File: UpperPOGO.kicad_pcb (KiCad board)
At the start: 2 copper layers, 128 x 58.5 mm, 29 parts, among them J1 Conn_01x01_MountingPin, J10 Conn_01x01_MountingPin, J11 Conn_01x01_MountingPin, J12 Conn_01x01_MountingPin, J13 Conn_01x01_MountingPin, J14 Conn_01x01_MountingPin, J15 Conn_01x01_MountingPin, J16 Conn_01x01_MountingPin, J17 Conn_01x01_MountingPin, J18 Conn_01x01_MountingPin, J19 Conn_01x01_MountingPin, J2 Conn_01x01_MountingPin, J20 Conn_01x01_MountingPin, J21 Conn_01x01_MountingPin, J22 Conn_01x01_MountingPin, J23 Conn_01x01_MountingPin, J24 Conn_01x01_MountingPin, J25 Conn_01x24_Pin, J3 Conn_01x01_MountingPin, J4 Conn_01x01_MountingPin, J5 Conn_01x01_MountingPin, J6 Conn_01x01_MountingPin, J7 Conn_01x01_MountingPin, J8 Conn_01x01_MountingPin, J9 Conn_01x01_MountingPin

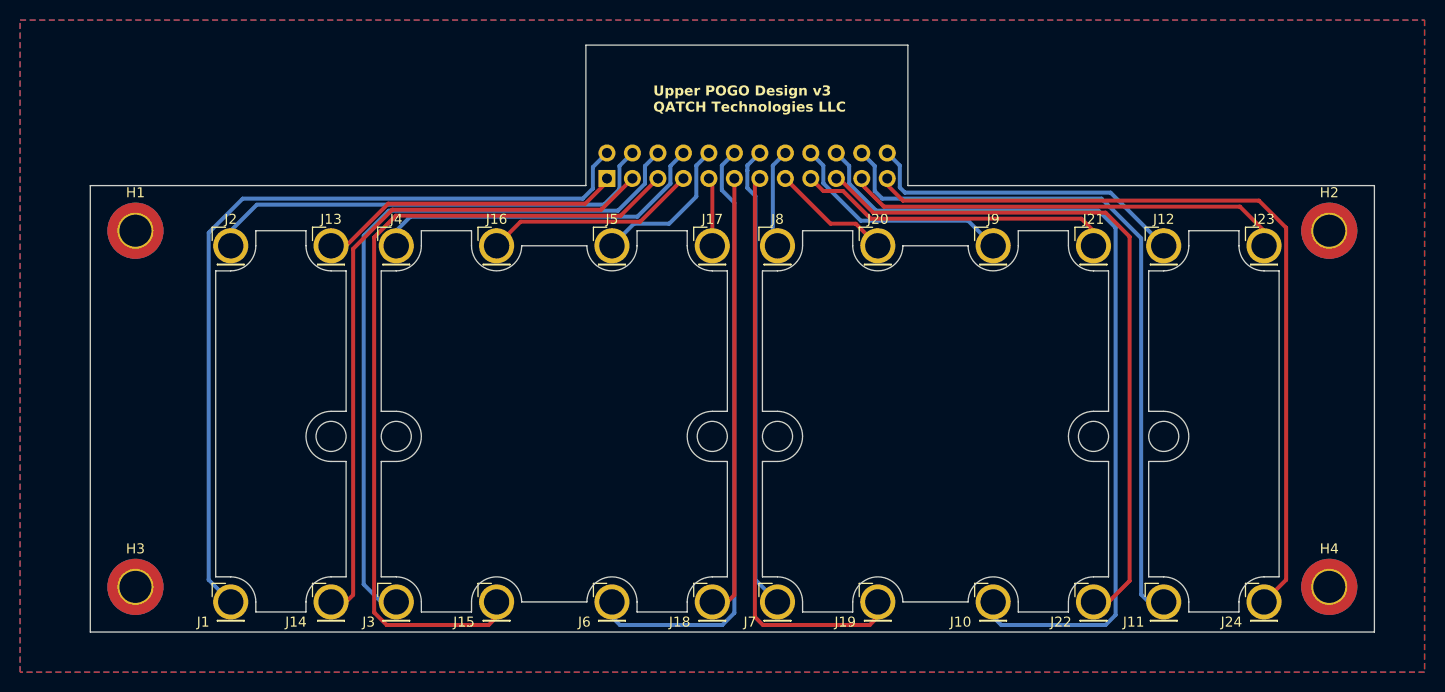
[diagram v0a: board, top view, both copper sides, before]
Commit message: Change footprint on J25 to vertical orientation header Resize PCB to remove unneeded area of horizontal silkscreening for J25 Update fabrication outputs and image renderings
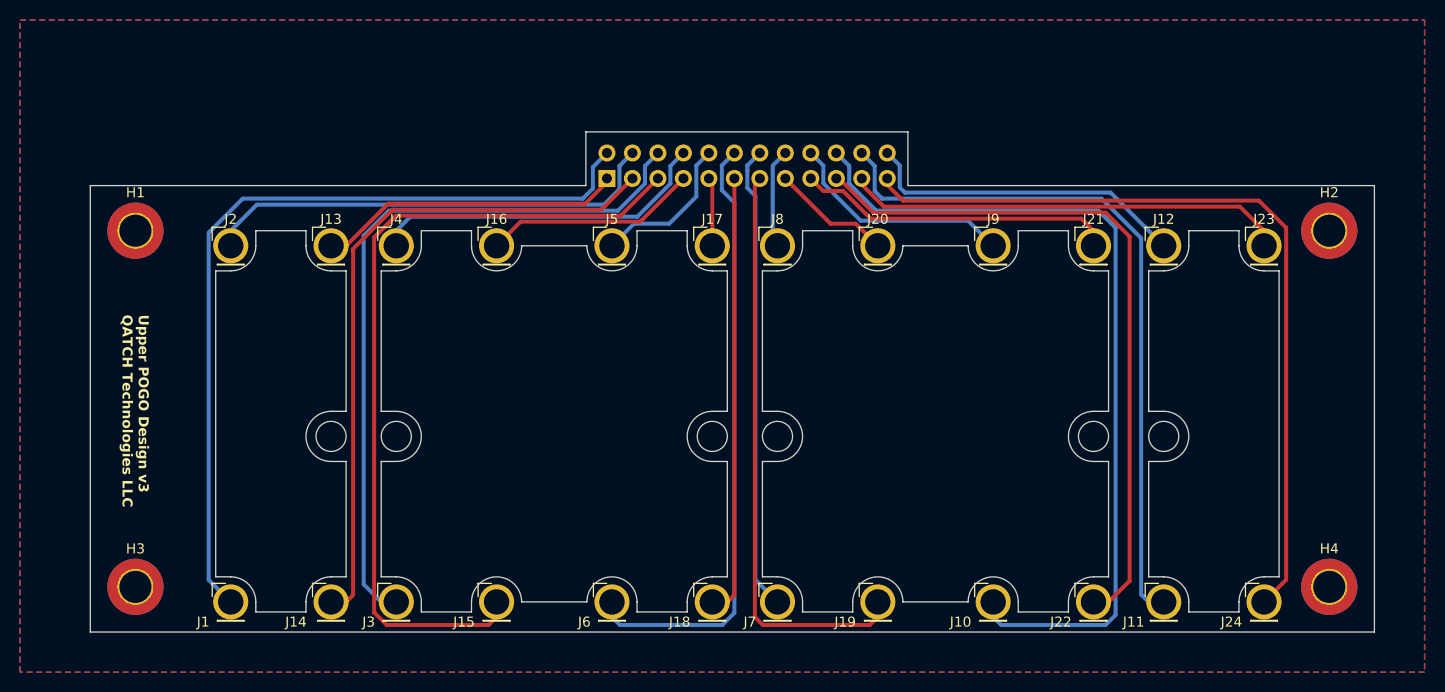
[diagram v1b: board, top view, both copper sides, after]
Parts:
- J25: footprint Connector_PinSocket_2.54mm:PinSocket_2x12_P2.54mm_Horizontal -> Connector_PinSocket_2.54mm:PinSocket_2x12_P2.54mm_Vertical
- moved J25 19.2 mm to (133.5, 60.8), turned to -90 degrees
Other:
- board size 128 x 58.5 mm -> 128 x 49.9 mm

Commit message: UpperPOGO v4 (2024-06-21) Resize J vias for proper fit inner diameter: 2.49mm outer diameter: 3.25mm
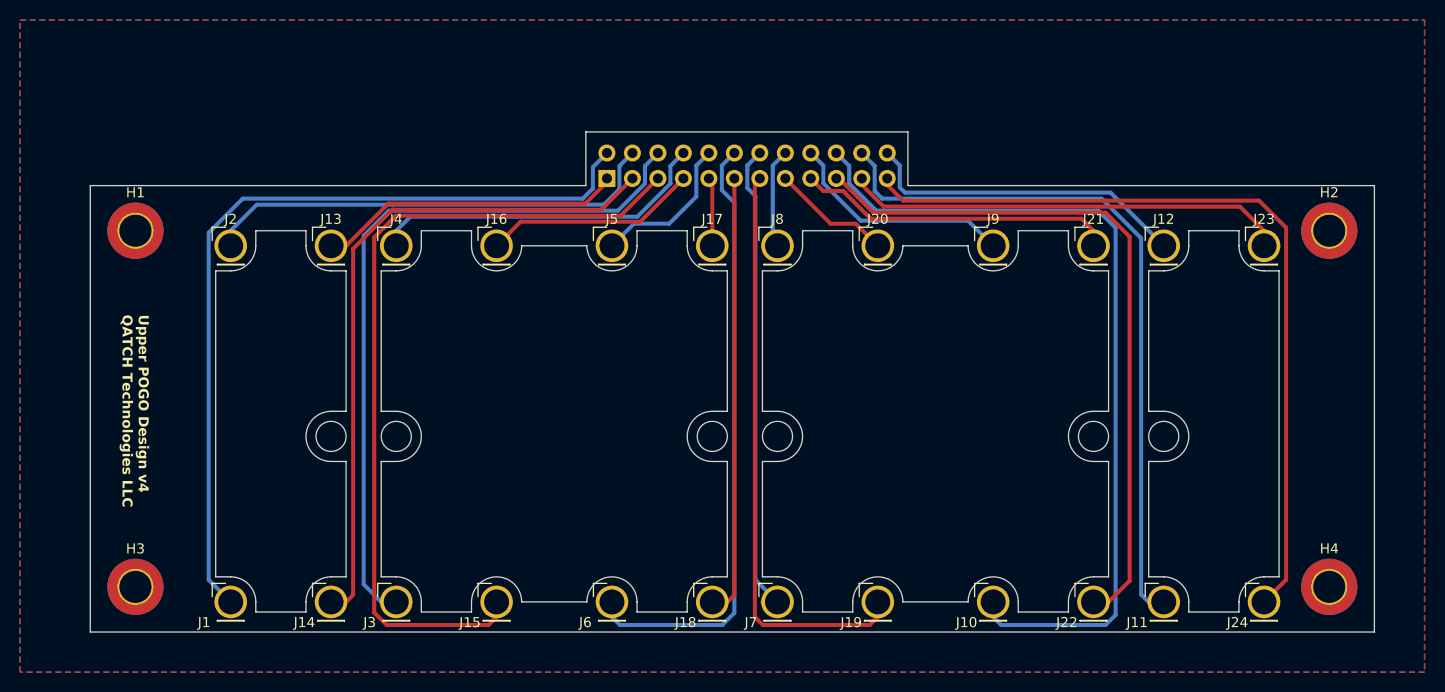
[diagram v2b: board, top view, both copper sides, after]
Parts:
- J1, J10, J11, J12, J13, J14, J15, J16, J17, J18, J19, J2, J20, J21, J22, J23, J24, J3, J4, J5, J6, J7, J8, J9: footprint Connector_PinHeader_2.54mm:PinHeader_1x01_D2.54mm_Vertical -> Connector_PinHeader_2.54mm:PinHeader_1x01_D2.54mm_Vertical_PogoPin
- J25: value Conn_01x24_Pin -> Conn_02x12_Pin
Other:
- board text added: "Upper POGO Design v4 QATCH Technologies LLC"
- board text removed: "Upper POGO Design v3 QATCH Technologies LLC"

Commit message: UpperPOGO v5 1mm trace spacing 1mm POGO clearance
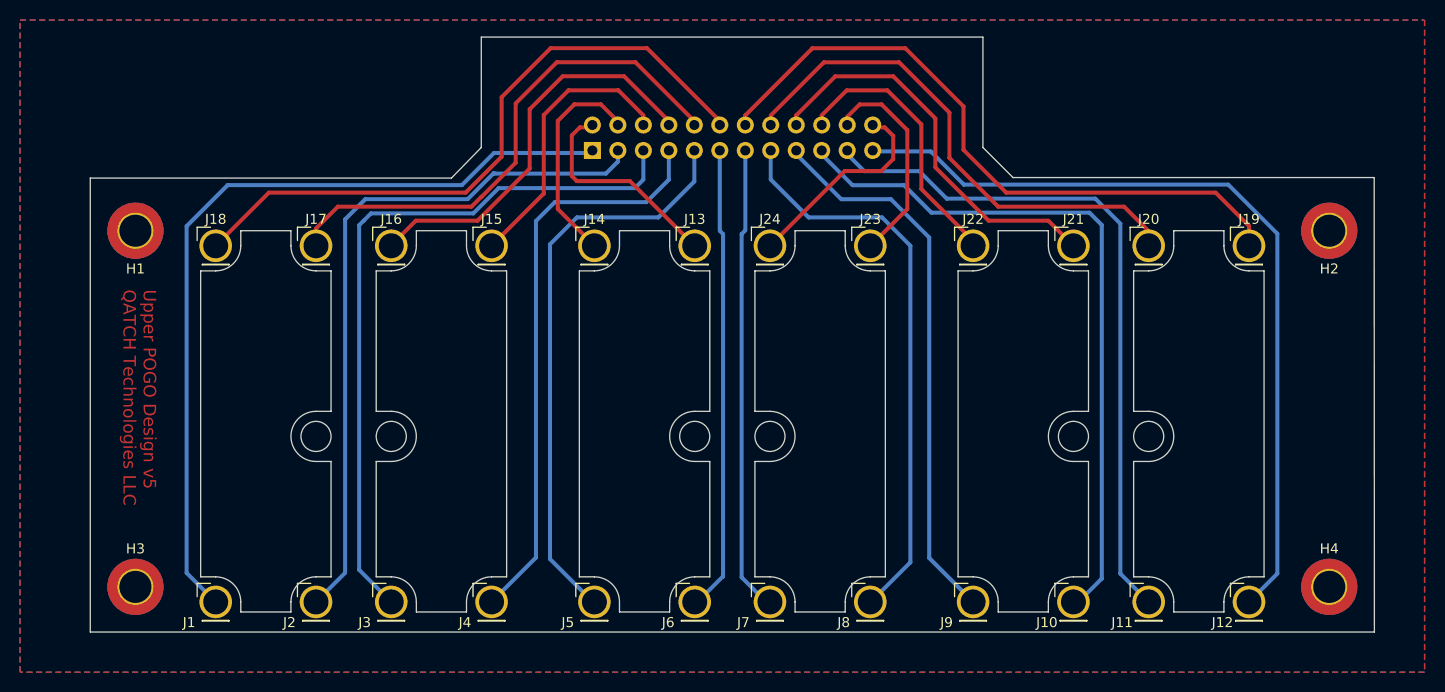
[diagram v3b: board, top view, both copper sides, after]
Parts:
- moved J25 3.14 mm to (132.1, 58.0)
- moved J10 2.00 mm to (180.0, 103.0)
- moved J21 2.00 mm to (180.0, 67.5)
- moved J22 2.00 mm to (170.0, 67.5)
- moved J9 2.00 mm to (170.0, 103.0)
- moved J13 1.75 mm to (142.2, 67.5)
- moved J14 1.75 mm to (132.2, 67.5)
- moved J5 1.75 mm to (132.2, 103.0)
- moved J6 1.75 mm to (142.2, 103.0)
- moved J1 1.50 mm to (94.5, 103.0)
- moved J11 1.50 mm to (187.5, 103.0)
- moved J12 1.50 mm to (197.5, 103.0)
- moved J17 1.50 mm to (104.5, 67.5)
- moved J18 1.50 mm to (94.5, 67.5)
- moved J19 1.50 mm to (197.5, 67.5)
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- renumbered J22 to J10, J24 to J12, J17 to J13, J5 to J14, J16 to J15, J4 to J16, J13 to J17, J2 to J18, J23 to J19, J14 to J2, J12 to J20, J9 to J22, J20 to J23, J8 to J24, J15 to J4, J6 to J5, J18 to J6, J19 to J8, J10 to J9
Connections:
- J10 pad 1: Net-(J22-Pin_1) -> Net-(J10-Pin_1)
- J12 pad 1: Net-(J24-Pin_1) -> Net-(J12-Pin_1)
- J13 pad 1: Net-(J17-Pin_1) -> Net-(J13-Pin_1)
- J14 pad 1: Net-(J25-Pin_5) -> Net-(J14-Pin_1)
- J15 pad 1: Net-(J16-Pin_1) -> Net-(J15-Pin_1)
- J16 pad 1: Net-(J25-Pin_4) -> Net-(J16-Pin_1)
- J17 pad 1: Net-(J13-Pin_1) -> Net-(J17-Pin_1)
- J18 pad 1: Net-(J2-Pin_1) -> Net-(J18-Pin_1)
- J19 pad 1: Net-(J23-Pin_1) -> Net-(J19-Pin_1)
- J2 pad 1: Net-(J14-Pin_1) -> Net-(J2-Pin_1)
- J20 pad 1: Net-(J12-Pin_1) -> Net-(J20-Pin_1)
- J22 pad 1: Net-(J25-Pin_9) -> Net-(J22-Pin_1)
- J23 pad 1: Net-(J20-Pin_1) -> Net-(J23-Pin_1)
- J24 pad 1: Net-(J25-Pin_8) -> Net-(J24-Pin_1)
- J4 pad 1: Net-(J15-Pin_1) -> Net-(J25-Pin_4)
- J5 pad 1: Net-(J25-Pin_6) -> Net-(J25-Pin_5)
- J6 pad 1: Net-(J18-Pin_1) -> Net-(J25-Pin_6)
- J8 pad 1: Net-(J19-Pin_1) -> Net-(J25-Pin_8)
- J9 pad 1: Net-(J10-Pin_1) -> Net-(J25-Pin_9)
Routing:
- net Net-(J24-Pin_1): track 80.4 -> 20.6 mm
- net Net-(J15-Pin_1): track 82.7 -> 28.1 mm
- net Net-(J12-Pin_1): track 32.7 -> 81.7 mm
- net Net-(J25-Pin_8): track 9.96 -> 56.4 mm
- net Net-(J14-Pin_1): track 67.7 -> 21.6 mm
- net Net-(J17-Pin_1): track 6.85 -> 52.2 mm
- net Net-(J22-Pin_1): track 70.4 -> 27.6 mm
- net Net-(J25-Pin_5): track 15.3 -> 57.4 mm
- net Net-(J20-Pin_1): track 12.0 -> 51.9 mm
- net Net-(J25-Pin_9): track 23.0 -> 54.8 mm
- net Net-(J2-Pin_1): track 46.1 -> 70.1 mm
- net Net-(J25-Pin_4): track 34.4 -> 57.4 mm
- net Net-(J23-Pin_1): track 44.1 -> 21.3 mm
- net Net-(J18-Pin_1): track 44.0 -> 65.5 mm
- net Net-(J16-Pin_1): track 21.4 -> 40.0 mm
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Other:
- board size 128 x 49.9 mm -> 128 x 59.3 mm
- board text added: "Upper POGO Design v5 QATCH Technologies LLC"
- board text removed: "Upper POGO Design v4 QATCH Technologies LLC"
